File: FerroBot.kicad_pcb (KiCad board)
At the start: 2 copper layers, 195.6 x 154.9 mm, 92 parts, among them J1 CONN_01X03, J10 CONN_01X03, J11 CONN_01X03, J12 CONN_01X03, J13 CONN_01X03, J14 CONN_01X03, J15 CONN_01X03, J16 CONN_01X03, J17 CONN_01X03, J18 CONN_01X03, J19 CONN_01X03, J2 CONN_01X03, J20 CONN_01X03, J21 CONN_01X03, J22 CONN_01X03, J23 CONN_01X03, J24 CONN_01X03, J25 CONN_01X03, J26 CONN_01X03, J27 CONN_01X03, J28 CONN_01X03, J29 CONN_01X03, J3 CONN_01X03, J30 CONN_01X03, J31 CONN_01X03, J32 CONN_01X03, J33 CONN_01X03, J34 CONN_01X03, J35 CONN_01X03, J36 CONN_01X03, J37 BARREL_JACK, J38 CONN_02X06, J39 CONN_01X01, J4 CONN_01X03, J40 CONN_01X01, J41 CONN_01X01, J42 CONN_01X01, J5 CONN_01X03, J6 CONN_01X03, J7 CONN_01X03, J8 CONN_01X03, J9 CONN_01X03, Q1 Q_NMOS_DGS, Q10 Q_NMOS_DGS, Q11 Q_NMOS_DGS, Q12 Q_NMOS_DGS, Q2 Q_NMOS_DGS, Q3 Q_NMOS_DGS, Q4 Q_NMOS_DGS, Q5 Q_NMOS_DGS, Q6 Q_NMOS_DGS, Q7 Q_NMOS_DGS, Q8 Q_NMOS_DGS, Q9 Q_NMOS_DGS, U1 Teensy_3.2

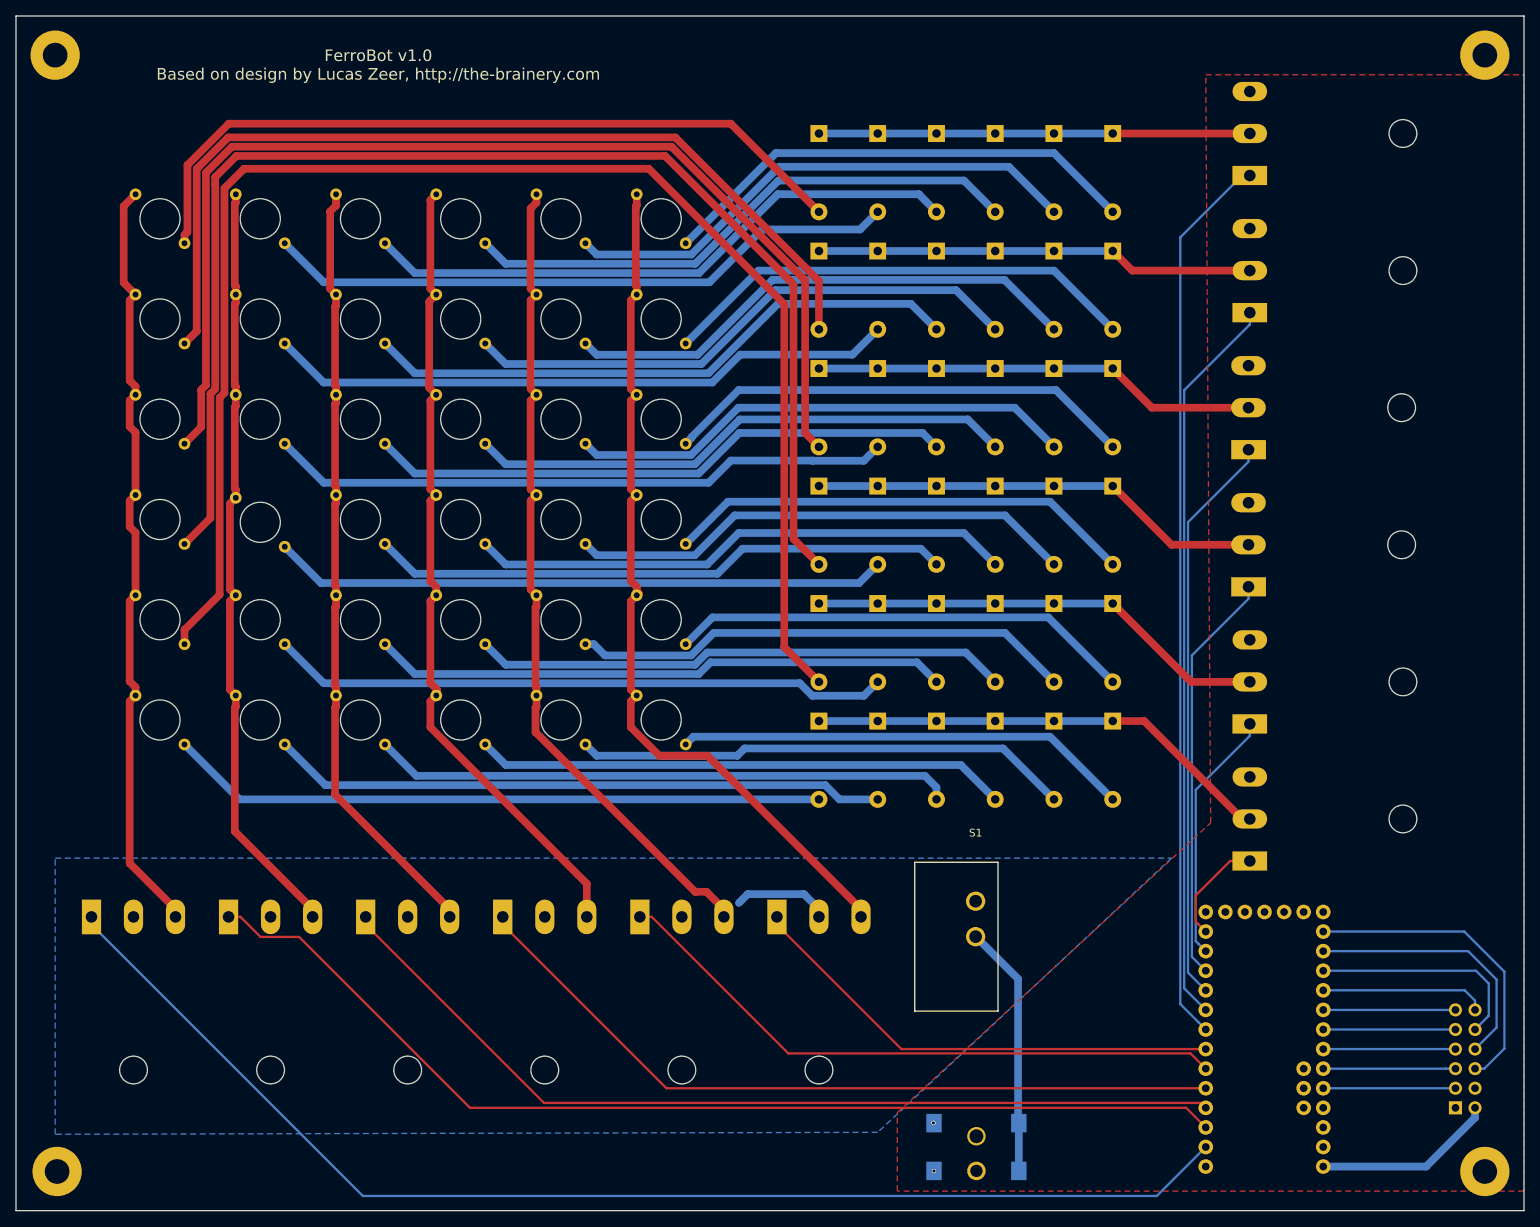
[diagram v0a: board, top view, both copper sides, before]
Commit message: Edit magnet footprint for better fit and shrink board
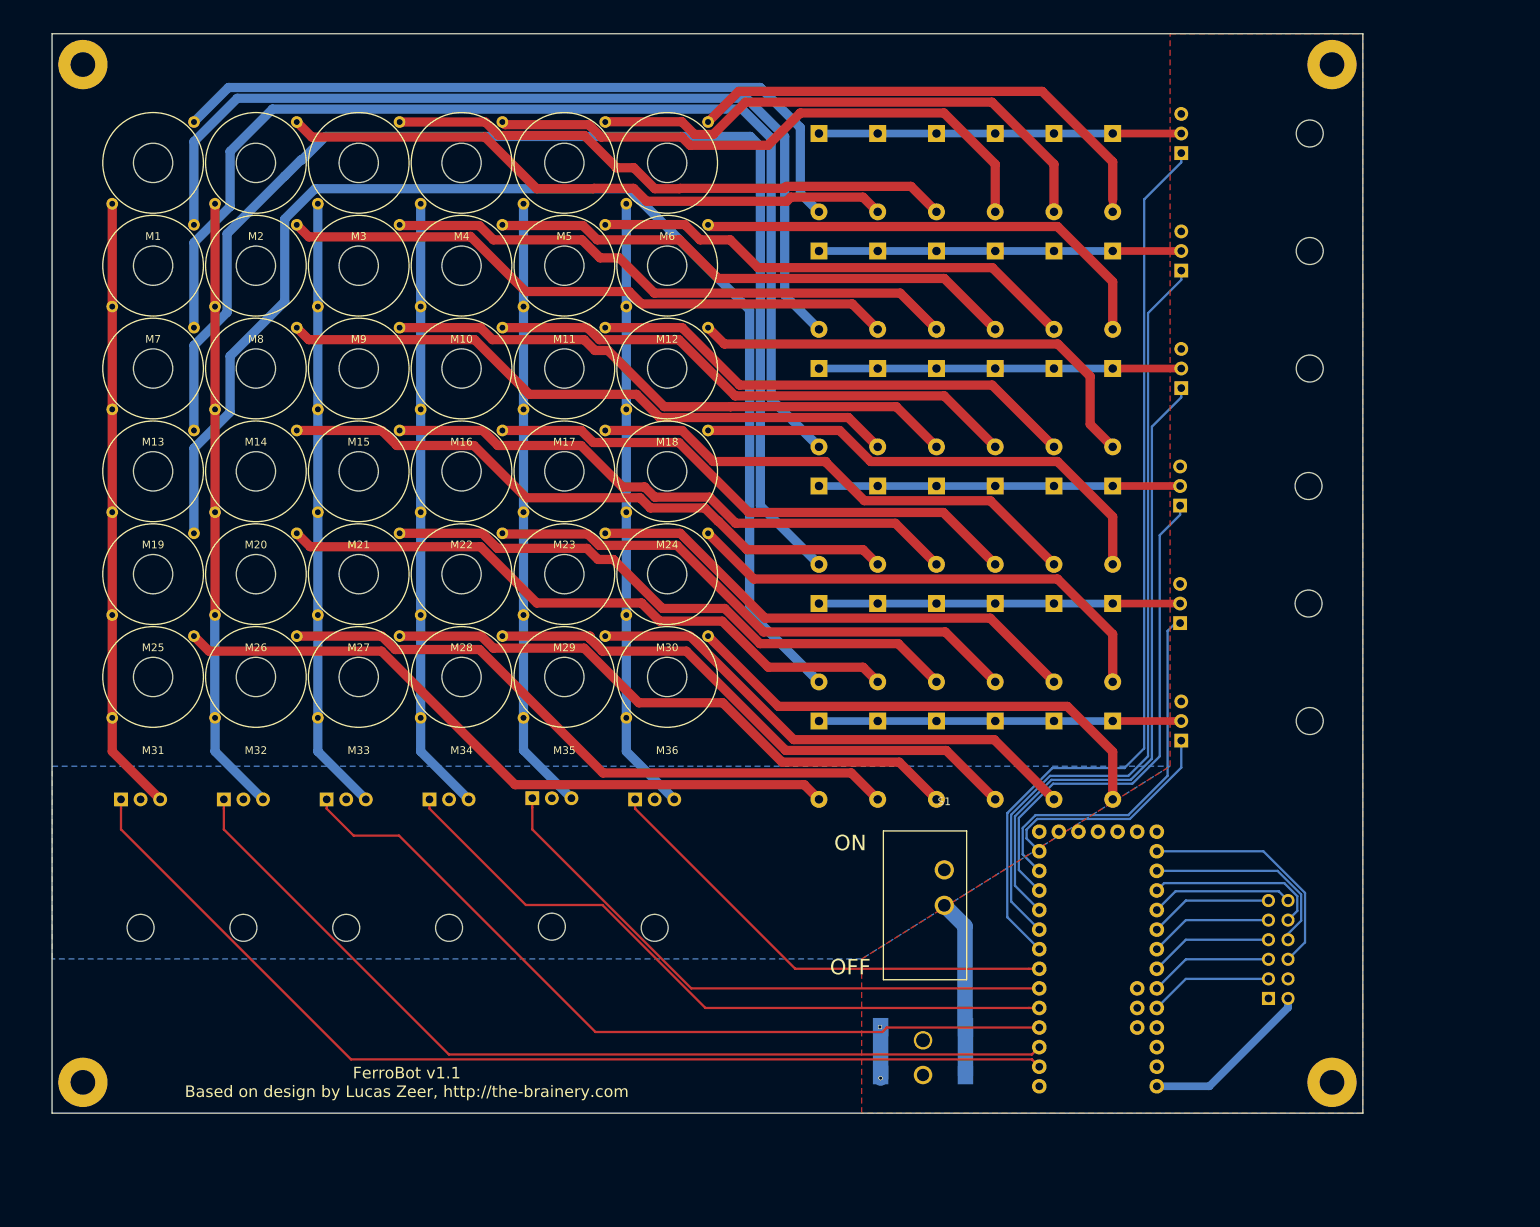
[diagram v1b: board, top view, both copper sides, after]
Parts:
- removed J1, J10, J11, J12, J13, J14, J15, J16, J17, J18, J19, J2, J20, J21, J22, J23, J24, J25, J26, J27, J28, J29, J3, J30, J31, J32, J33, J34, J35, J36, J4, J5, J6, J7, J8, J9: CONN_01X03, WheelerLab:Ferrobot_Magnet
- added M1: FERROBOT_MAGNET, WheelerLab:Ferrobot_Magnet, F.Cu at (38.1, 31.8)
- added M10: FERROBOT_MAGNET, WheelerLab:Ferrobot_Magnet, F.Cu at (78.1, 45.1)
- added M11: FERROBOT_MAGNET, WheelerLab:Ferrobot_Magnet, F.Cu at (91.4, 45.1)
- added M12: FERROBOT_MAGNET, WheelerLab:Ferrobot_Magnet, F.Cu at (104.8, 45.1)
- added M13: FERROBOT_MAGNET, WheelerLab:Ferrobot_Magnet, F.Cu at (38.1, 58.4)
- added M14: FERROBOT_MAGNET, WheelerLab:Ferrobot_Magnet, F.Cu at (51.4, 58.4)
- added M15: FERROBOT_MAGNET, WheelerLab:Ferrobot_Magnet, F.Cu at (64.8, 58.4)
- added M16: FERROBOT_MAGNET, WheelerLab:Ferrobot_Magnet, F.Cu at (78.1, 58.4)
- added M17: FERROBOT_MAGNET, WheelerLab:Ferrobot_Magnet, F.Cu at (91.4, 58.4)
- added M18: FERROBOT_MAGNET, WheelerLab:Ferrobot_Magnet, F.Cu at (104.8, 58.4)
- added M19: FERROBOT_MAGNET, WheelerLab:Ferrobot_Magnet, F.Cu at (38.1, 71.8)
- added M2: FERROBOT_MAGNET, WheelerLab:Ferrobot_Magnet, F.Cu at (51.4, 31.8)
- added M20: FERROBOT_MAGNET, WheelerLab:Ferrobot_Magnet, F.Cu at (51.4, 71.8)
- added M21: FERROBOT_MAGNET, WheelerLab:Ferrobot_Magnet, F.Cu at (64.8, 71.8)
- added M22: FERROBOT_MAGNET, WheelerLab:Ferrobot_Magnet, F.Cu at (78.1, 71.8)
- added M23: FERROBOT_MAGNET, WheelerLab:Ferrobot_Magnet, F.Cu at (91.4, 71.8)
- added M24: FERROBOT_MAGNET, WheelerLab:Ferrobot_Magnet, F.Cu at (104.8, 71.8)
- added M25: FERROBOT_MAGNET, WheelerLab:Ferrobot_Magnet, F.Cu at (38.1, 85.1)
- added M26: FERROBOT_MAGNET, WheelerLab:Ferrobot_Magnet, F.Cu at (51.4, 85.1)
- added M27: FERROBOT_MAGNET, WheelerLab:Ferrobot_Magnet, F.Cu at (64.8, 85.1)
- added M28: FERROBOT_MAGNET, WheelerLab:Ferrobot_Magnet, F.Cu at (78.1, 85.1)
- added M29: FERROBOT_MAGNET, WheelerLab:Ferrobot_Magnet, F.Cu at (91.4, 85.1)
- added M3: FERROBOT_MAGNET, WheelerLab:Ferrobot_Magnet, F.Cu at (64.8, 31.8)
- added M30: FERROBOT_MAGNET, WheelerLab:Ferrobot_Magnet, F.Cu at (104.8, 85.1)
- added M31: FERROBOT_MAGNET, WheelerLab:Ferrobot_Magnet, F.Cu at (38.1, 98.4)
- added M32: FERROBOT_MAGNET, WheelerLab:Ferrobot_Magnet, F.Cu at (51.4, 98.4)
- added M33: FERROBOT_MAGNET, WheelerLab:Ferrobot_Magnet, F.Cu at (64.8, 98.4)
- added M34: FERROBOT_MAGNET, WheelerLab:Ferrobot_Magnet, F.Cu at (78.1, 98.4)
- added M35: FERROBOT_MAGNET, WheelerLab:Ferrobot_Magnet, F.Cu at (91.4, 98.4)
- added M36: FERROBOT_MAGNET, WheelerLab:Ferrobot_Magnet, F.Cu at (104.8, 98.4)
- added M4: FERROBOT_MAGNET, WheelerLab:Ferrobot_Magnet, F.Cu at (78.1, 31.8)
- added M5: FERROBOT_MAGNET, WheelerLab:Ferrobot_Magnet, F.Cu at (91.4, 31.8)
- added M6: FERROBOT_MAGNET, WheelerLab:Ferrobot_Magnet, F.Cu at (104.8, 31.8)
- added M7: FERROBOT_MAGNET, WheelerLab:Ferrobot_Magnet, F.Cu at (38.1, 45.1)
- added M8: FERROBOT_MAGNET, WheelerLab:Ferrobot_Magnet, F.Cu at (51.4, 45.1)
- added M9: FERROBOT_MAGNET, WheelerLab:Ferrobot_Magnet, F.Cu at (64.8, 45.1)
- Q1, Q10, Q11, Q12, Q2, Q3, Q4, Q5, Q6, Q7, Q8, Q9: footprint TO_SOT_Packages_THT:TO-247_TO-3P_Horizontal -> TO_SOT_Packages_THT:TO-220-3_Horizontal
- moved J38 28.1 mm to (182.8, 140.1)
- moved U1 24.0 mm to (160.7, 135.3)
- moved Q12 23.9 mm to (100.6, 114.3)
- moved J42 22.9 mm to (191.0, 151.0)
- moved Q11 20.8 mm to (87.3, 114.2)
- moved J39 19.9 mm to (191.0, 19.0)
- moved Q6 18.0 mm to (171.4, 106.7)
- moved Q10 18.0 mm to (73.9, 114.3)
- moved Q9 16.1 mm to (60.6, 114.3)
- moved Q5 15.9 mm to (171.3, 91.4)
- moved Q7 15.7 mm to (33.9, 114.3)
- moved Q8 15.3 mm to (47.3, 114.3)
- moved J37 14.2 mm to (138.0, 150.0)
- moved Q4 13.8 mm to (171.3, 76.2)
- moved J41 12.0 mm to (29.0, 151.0)
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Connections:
- J38 pad 4: (no net) -> Net-(J38-Pad4)
- J39 pad 1: (no net) -> Net-(J39-Pad1)
- J40 pad 1: (no net) -> Net-(J40-Pad1)
- J41 pad 1: (no net) -> Net-(J41-Pad1)
- J42 pad 1: (no net) -> Net-(J42-Pad1)
- Q8 pad 2: PWR -> Net-(Q8-Pad2)
- U1 pad 12: (no net) -> Net-(U1-Pad12)
- U1 pad 13: (no net) -> Net-(U1-Pad13)
- U1 pad 23: (no net) -> Net-(U1-Pad23)
- U1 pad 24: (no net) -> Net-(U1-Pad24)
- U1 pad 25: (no net) -> Net-(U1-Pad25)
- U1 pad 28: (no net) -> Net-(U1-Pad28)
- U1 pad 29: (no net) -> Net-(U1-Pad29)
- U1 pad 31: (no net) -> Net-(U1-Pad31)
- U1 pad 32: (no net) -> Net-(U1-Pad32)
- U1 pad 33: (no net) -> Net-(U1-Pad33)
- U1 pad 34: (no net) -> Net-(U1-Pad34)
- U1 pad 35: (no net) -> Net-(U1-Pad35)
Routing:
- net ROW6: track 113.4 -> 80.1 mm
- net R1CONTROL: track 163.7 -> 135.7 mm
- net ROW5: track 107.4 -> 80.0 mm
- net DIODE25: track 193.0 -> 166.0 mm
- net ROW4: track 105.8 -> 80.1 mm
- net ROW3: track 101.0 -> 80.1 mm
- net ROW1: track 100.5 -> 80.1 mm
- net ROW2: track 99.5 -> 80.1 mm
- net C5CONTROL: track 32.9 -> 49.5 mm
- net C6CONTROL: track 14.2 -> 30.4 mm
- net R2CONTROL: track 138.0 -> 122.1 mm
- net COLUMN6: track 61.1 -> 47.0 mm
- net R3CONTROL: track 119.8 -> 105.9 mm
- net COLUMN5: track 60.1 -> 46.8 mm
- net PWR: track 12.7 -> 0.00 mm
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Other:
- board size 195.6 x 154.9 mm -> 170 x 140 mm
- net class big: trace_width 1 -> 1.2
- board text added: "FerroBot v1.1 Based on design by Lucas Zeer, http://the-brainery.com"
- board text added: "ON OFF"
- board text removed: "FerroBot v1.0 Based on design by Lucas Zeer, http://the-brainery.com"

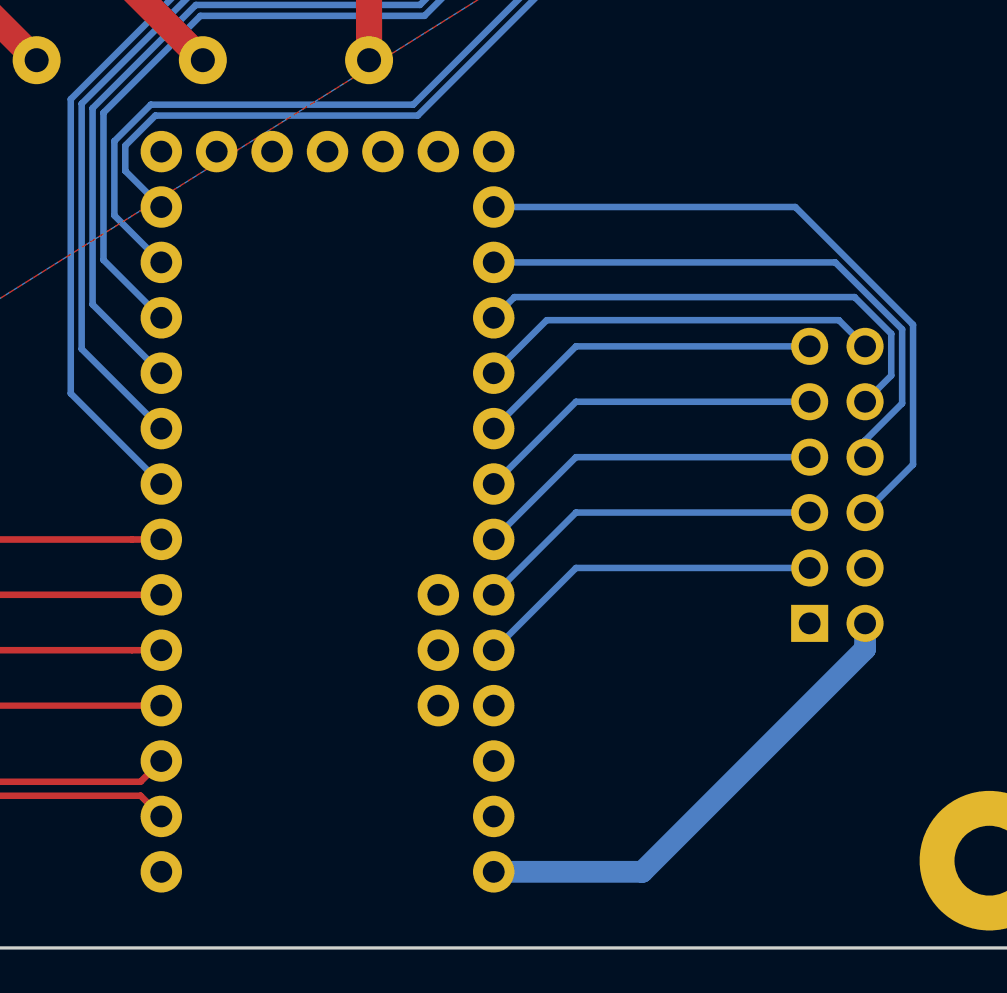
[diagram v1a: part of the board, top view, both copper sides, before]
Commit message: Moved Teensy version to new branch, master now has generic connections to be used for any arduino
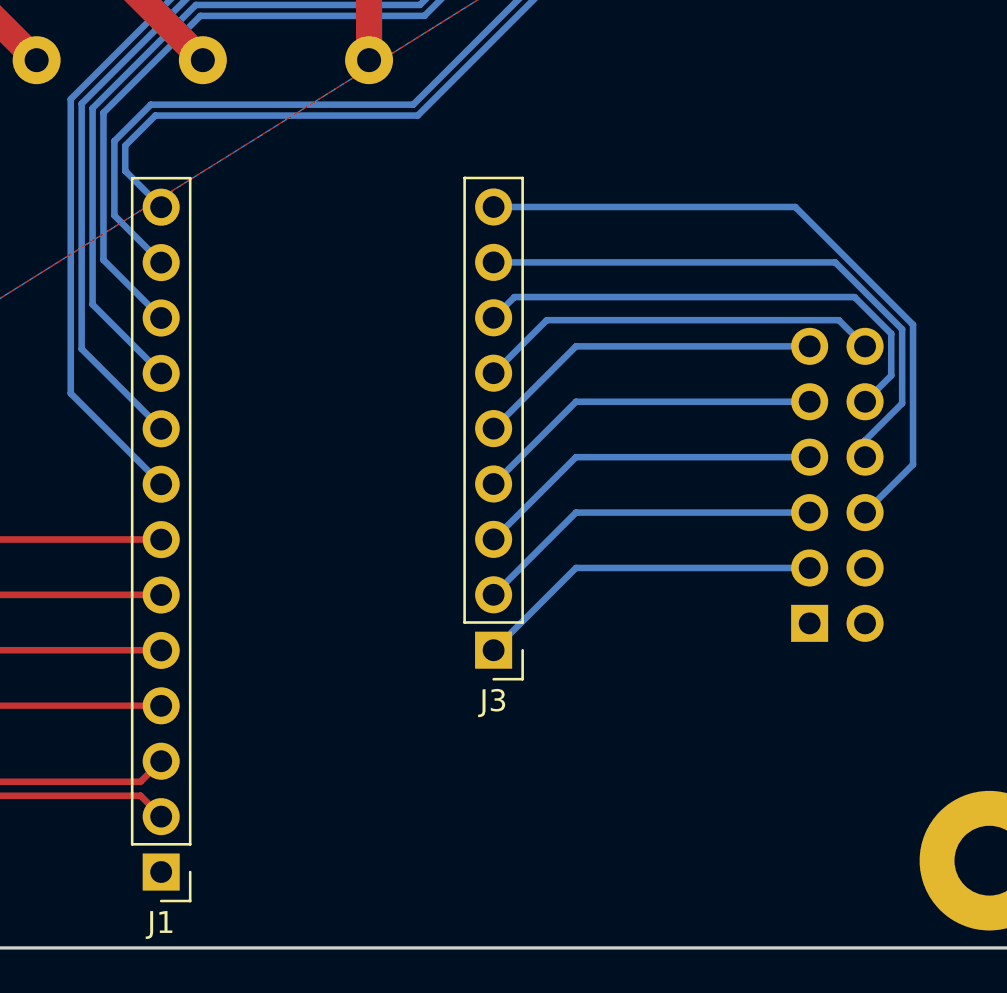
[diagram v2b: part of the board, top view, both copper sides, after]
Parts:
- removed U1: Teensy_3.2, WheelerLab:Teensy-3.2
- added J1: Conn_01x13, Pin_Headers:Pin_Header_Straight_1x13_Pitch2.54mm, F.Cu at (153.0, 151.5)
- added J3: Conn_01x09, Pin_Headers:Pin_Header_Straight_1x09_Pitch2.54mm, F.Cu at (168.3, 141.3)
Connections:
- J38 pad 2: Vin -> Net-(J38-Pad2)
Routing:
- net Vin: track 22.4 -> 0.00 mm
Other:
- board text added: "GND"
- board text added: "In from Arduino"
- board text added: "Out to Arduino"
